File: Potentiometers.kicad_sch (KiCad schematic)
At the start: 14 parts, among them J12 Brake_Sw, J7 Accel_Pot, J9 Brake_Pot

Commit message: Replaced unavailable parts
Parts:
- R14: Mouser Part Number (none) -> 71-CRCW0805100KFKEAC
- R15: Mouser Part Number 71-CRCW080510K0FKEAC -> 71-CRCW08054K99FKEAC
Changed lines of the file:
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@@
 			)
 		)
-		(property "Mouser Part Number" "71-CRCW080510K0FKEAC "
+		(property "Mouser Part Number" "71-CRCW08054K99FKEAC "
 			(at 110.49 80.01 0)
 			(effects
@@
 			)
 		)
-		(property "Mouser Part Number" ""
+		(property "Mouser Part Number" "71-CRCW0805100KFKEAC"
 			(at 93.98 83.82 0)
 			(effects

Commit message: Filled in part numbers, exported BOM and made Excel file for working with it.
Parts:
- C16, C17: P/N (none) -> C0805C104M5R
- D2, D3: P/N (none) -> CDSOT23-T24CAN
- J12: P/N (none) -> 436500215
- J7, J9: P/N (none) -> 436500315
- R14: P/N Inventory -> CRCW0805100KFKEAC
- R15: P/N (none) -> CRCW08054K99FKEAC
- R16, R26, R27: P/N (none) -> CRCW080510K0FKEAC
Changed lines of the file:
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@@
+			)
+		)
+		(property "P/N" "CDSOT23-T24CAN"
+			(at 101.6 83.82 0)
+			(effects
+				(font
+					(size 1.27 1.27)
+				)
+				(hide yes)
 			)
 		)
@@
 			)
 		)
+		(property "P/N" "CDSOT23-T24CAN"
+			(at 101.6 116.84 0)
+			(effects
+				(font
+					(size 1.27 1.27)
+				)
+				(hide yes)
+			)
+		)
 		(pin "2"
 		)
@@
 			)
 		)
+		(property "P/N" "C0805C104M5R"
+			(at 83.82 83.82 0)
+			(effects
+				(font
+					(size 1.27 1.27)
+				)
+				(hide yes)
+			)
+		)
 		(pin "1"
 		)
@@
 			)
 		)
+		(property "P/N" "CRCW080510K0FKEAC "
+			(at 110.49 113.03 0)
+			(effects
+				(font
+					(size 1.27 1.27)
+				)
+				(hide yes)
+			)
+		)
 		(pin "1"
 		)
@@
 			)
 		)
+		(property "P/N" "C0805C104M5R"
+			(at 83.82 116.84 0)
+			(effects
+				(font
+					(size 1.27 1.27)
+				)
+				(hide yes)
+			)
+		)
 		(pin "1"
 		)
@@
 			)
 		)
+		(property "P/N" "CDSOT23-T24CAN"
+			(at 101.6 74.93 0)
+			(effects
+				(font
+					(size 1.27 1.27)
+				)
+				(hide yes)
+			)
+		)
 		(pin "2"
 		)
@@
 			)
 		)
+		(property "P/N" "CDSOT23-T24CAN"
+			(at 101.6 107.95 0)
+			(effects
+				(font
+					(size 1.27 1.27)
+				)
+				(hide yes)
+			)
+		)
 		(pin "2"
 		)
@@
 			)
 		)
+		(property "P/N" "CRCW08054K99FKEAC "
+			(at 110.49 80.01 0)
+			(effects
+				(font
+					(size 1.27 1.27)
+				)
+				(hide yes)
+			)
+		)
 		(pin "1"
 		)
@@
 			)
 		)
-		(property "P/N" "Inventory"
+		(property "P/N" "CRCW0805100KFKEAC"
 			(at 93.98 83.82 0)
 			(effects
@@
 			)
 		)
+		(property "P/N" "CRCW080510K0FKEAC "
+			(at 114.3 147.32 0)
+			(effects
+				(font
+					(size 1.27 1.27)
+				)
+				(hide yes)
+			)
+		)
 		(pin "1"
 		)
@@
 			)
 		)
-		(property "Datasheet" "~"
+		(property "Datasheet" "https://www.molex.com/en-us/products/part-detail/436500215"
 			(at 129.54 138.43 0)
 			(effects
@@
 		)
 		(property "Description" "Generic connector, single row, 01x02, script generated (kicad-library-utils/schlib/autogen/connector/)"
+			(at 129.54 138.43 0)
+			(effects
+				(font
+					(size 1.27 1.27)
+				)
+				(hide yes)
+			)
+		)
+		(property "P/N" "436500215"
 			(at 129.54 138.43 0)
 			(effects
@@
 			)
 		)
-		(property "Datasheet" "~"
+		(property "Datasheet" "https://www.molex.com/molex/search/partSearch?query=436500315&pQuery="
 			(at 144.78 113.03 0)
 			(effects
@@
 		)
 		(property "Vds" ""
+			(at 144.78 113.03 0)
+			(effects
+				(font
+					(size 1.27 1.27)
+				)
+				(hide yes)
+			)
+		)
+		(property "P/N" "436500315"
 			(at 144.78 113.03 0)
 			(effects
@@
 			)
 		)
+		(property "P/N" "CRCW080510K0FKEAC "
+			(at 106.68 140.97 0)
+			(effects
+				(font
+					(size 1.27 1.27)
+				)
+				(hide yes)
+			)
+		)
 		(pin "1"
 		)
@@
 			)
 		)
-		(property "Datasheet" "~"
+		(property "Datasheet" "https://www.molex.com/molex/search/partSearch?query=436500315&pQuery="
 			(at 144.78 80.01 0)
 			(effects
@@
 			(at 144.78 80.01 0)
 			(effects
+				(font
+					(size 1.27 1.27)
+				)
+				(hide yes)
+			)
+		)
+		(property "P/N" "436500315"
+			(at 144.78 80.01 0)
+			(effects

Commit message: Added version update notes.
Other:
- note added: "- Updated accel pot values to increase ADC range - Added brake switch button circuit"
- note removed: "Added brake pot, updated accel pot resistor values"
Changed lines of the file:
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@@
 		)
 	)
-	(text "Added brake pot, updated accel pot resistor values"
+	(text "- Updated accel pot values to increase ADC range\n- Added brake switch button circuit "
 		(exclude_from_sim no)
 		(at 177.8 180.086 0)

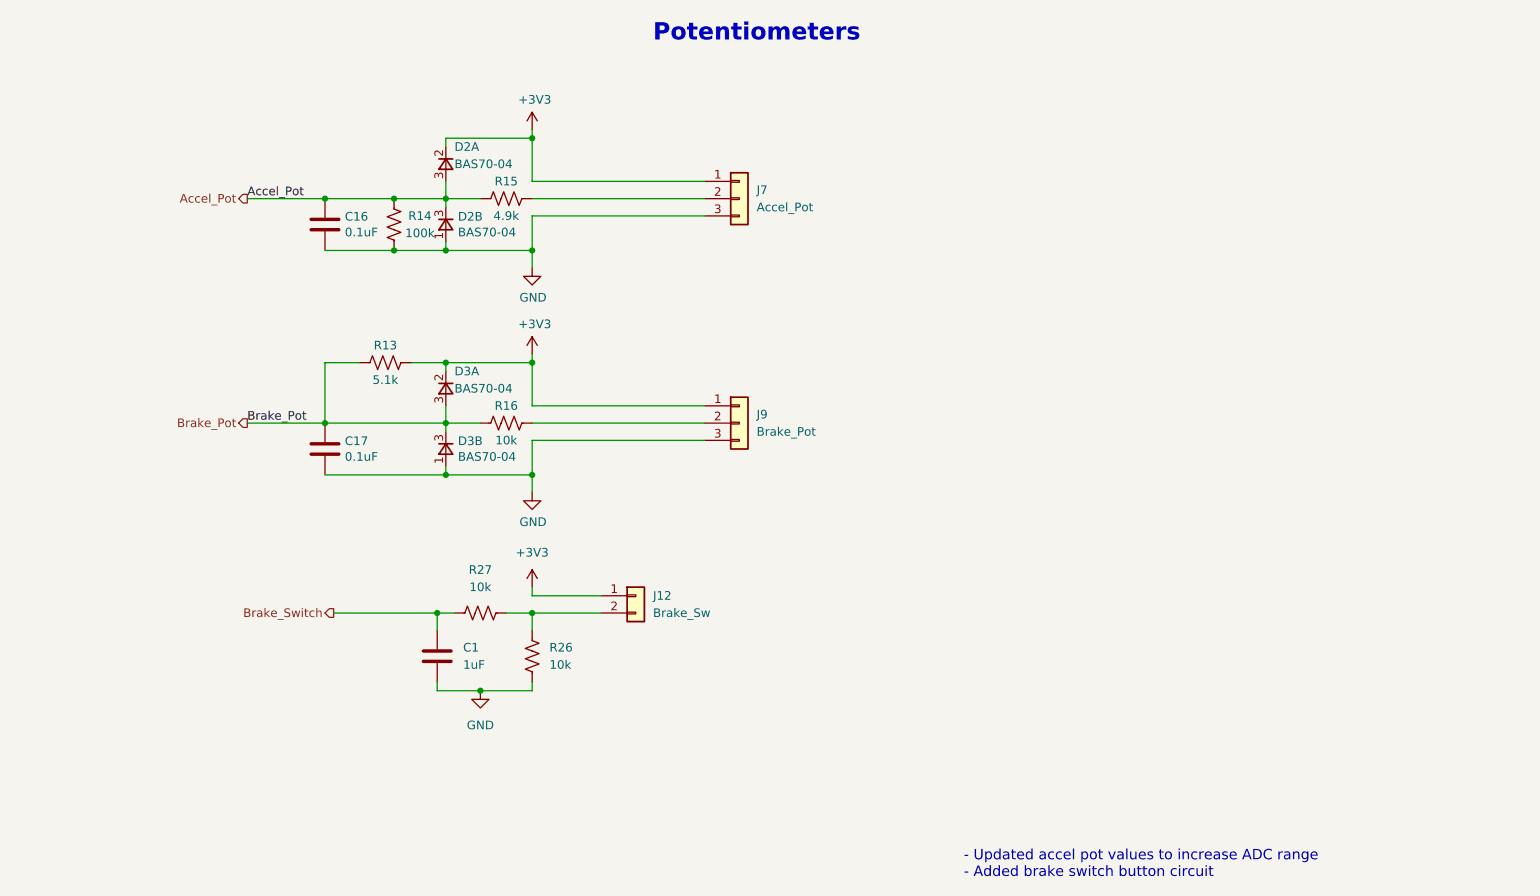
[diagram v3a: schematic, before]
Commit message: Added resistor divider to support 5V potentiometer
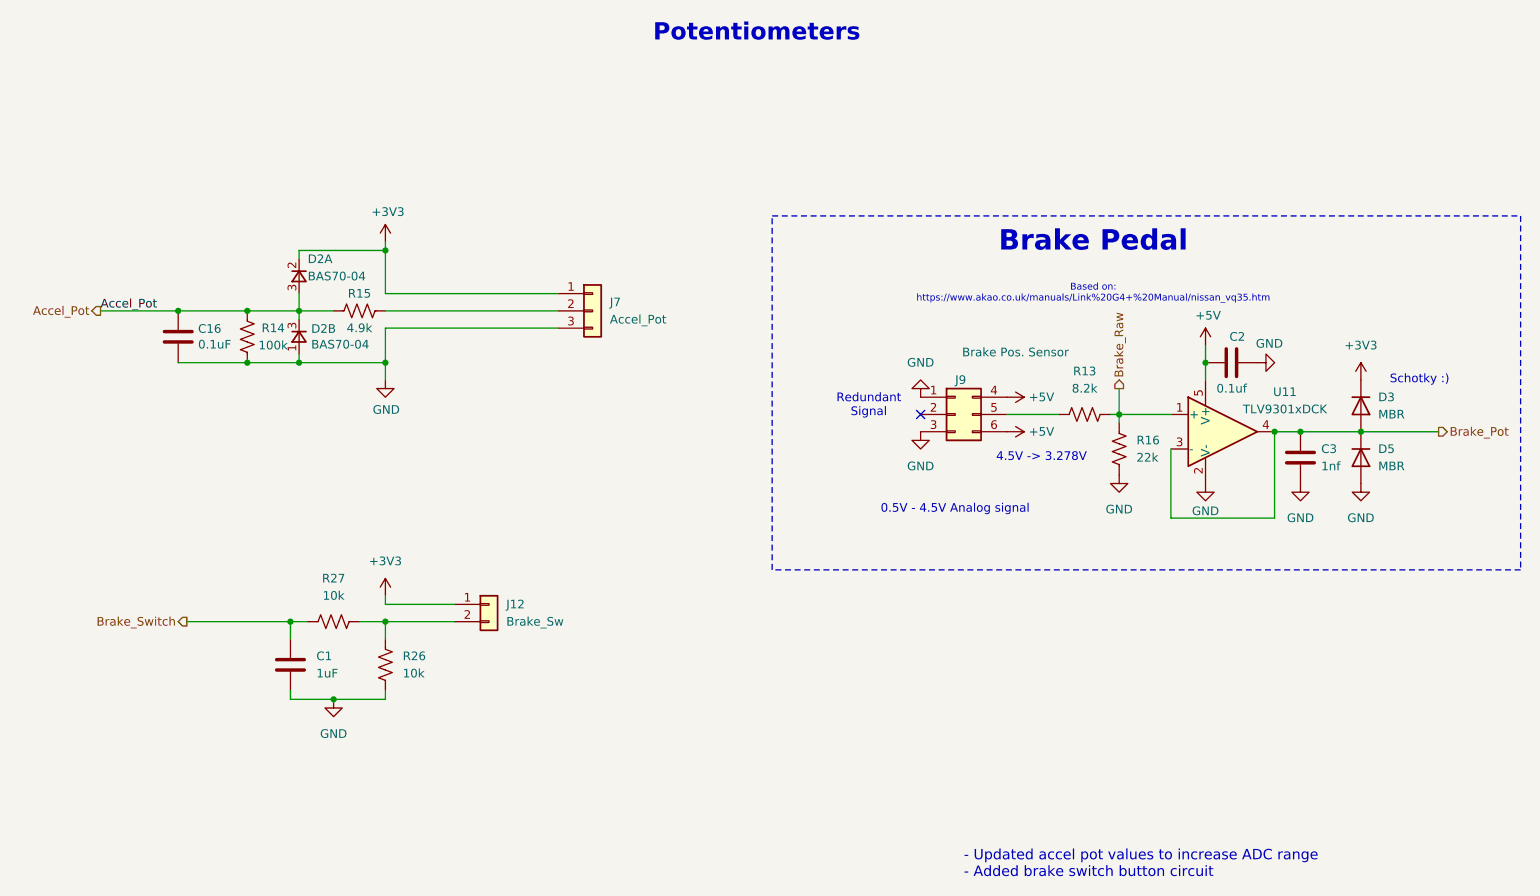
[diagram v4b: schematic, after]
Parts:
- removed C17: 0.1uF, Capacitor_SMD:C_0805_2012Metric, symbol Device:C
- removed D3: BAS70-04, Package_TO_SOT_SMD:SOT-23, symbol utsvt-chips:BAS70-04
- removed J9: Brake_Pot, Connector_Molex:Molex_Micro-Fit_3.0_43650-0315_1x03_P3.00mm_Vertical, symbol Connector_Generic:Conn_01x03
- added C2: 0.1uf, Capacitor_SMD:C_0805_2012Metric, symbol Device:C
- added C3: 1nf, Capacitor_SMD:C_0805_2012Metric, symbol Device:C
- added D3, D5: MBR, Diode_SMD:D_0805_2012Metric, symbol Device:D
- added J9: Brake Pos. Sensor, Connector_Molex:Molex_Micro-Fit_3.0_43045-0612_2x03_P3.00mm_Vertical, symbol Connector_Generic:Conn_02x03_Top_Bottom
- added U11: TLV9301xDCK, Package_TO_SOT_SMD:SOT-353_SC-70-5, symbol Amplifier_Operational:TLV9301xDCK
- R13: value 5.1k -> 8.2k; P/N Inventory -> ERA-3ARB822V
- R16: value 10k -> 22k; Mouser Part Number 71-CRCW080510K0FKEAC -> (none); P/N CRCW080510K0FKEAC -> pickle
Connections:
- net +3V3: now also D3.1 (K); no longer R13.1
- net Brake_Pot: now also C3.2, D3.2 (A), D5.1 (K), U11.3 (-), U11.4; no longer R13.2, R16.2
- net GND: now also R16.2, C2.1, C3.1, D5.2 (A), J9.1 (Pin_1), J9.3 (Pin_3), U11.2 (V-)
- net Brake_Raw: now reaches R16.1
- net Brake_Raw: now also R13.1, U11.1 (+)
- new net: J9.5 (Pin_5), R13.2
- new net +5V: C2.2, J9.4 (Pin_4), J9.6 (Pin_6), U11.5 (V+)
- no-connect marks 0 -> 1
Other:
- note added: "0.5V - 4.5V Analog signal"
- note added: "4.5V -> 3.278V"
- note added: "Based on: https://www.akao.co.uk/manuals/Link%20G4+%20Manual/nissan_vq35.htm"
- note added: "Brake Pedal"
- note added: "Redundant Signal"
- note added: "Schotky :)"
- moved on the sheet: C1, C16, D2A, D2B, J12, J7, R14, R15, R26, R27

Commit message: Removed precharge contactor stuff, made accel 5V instead of 3, removed op amp for brake.
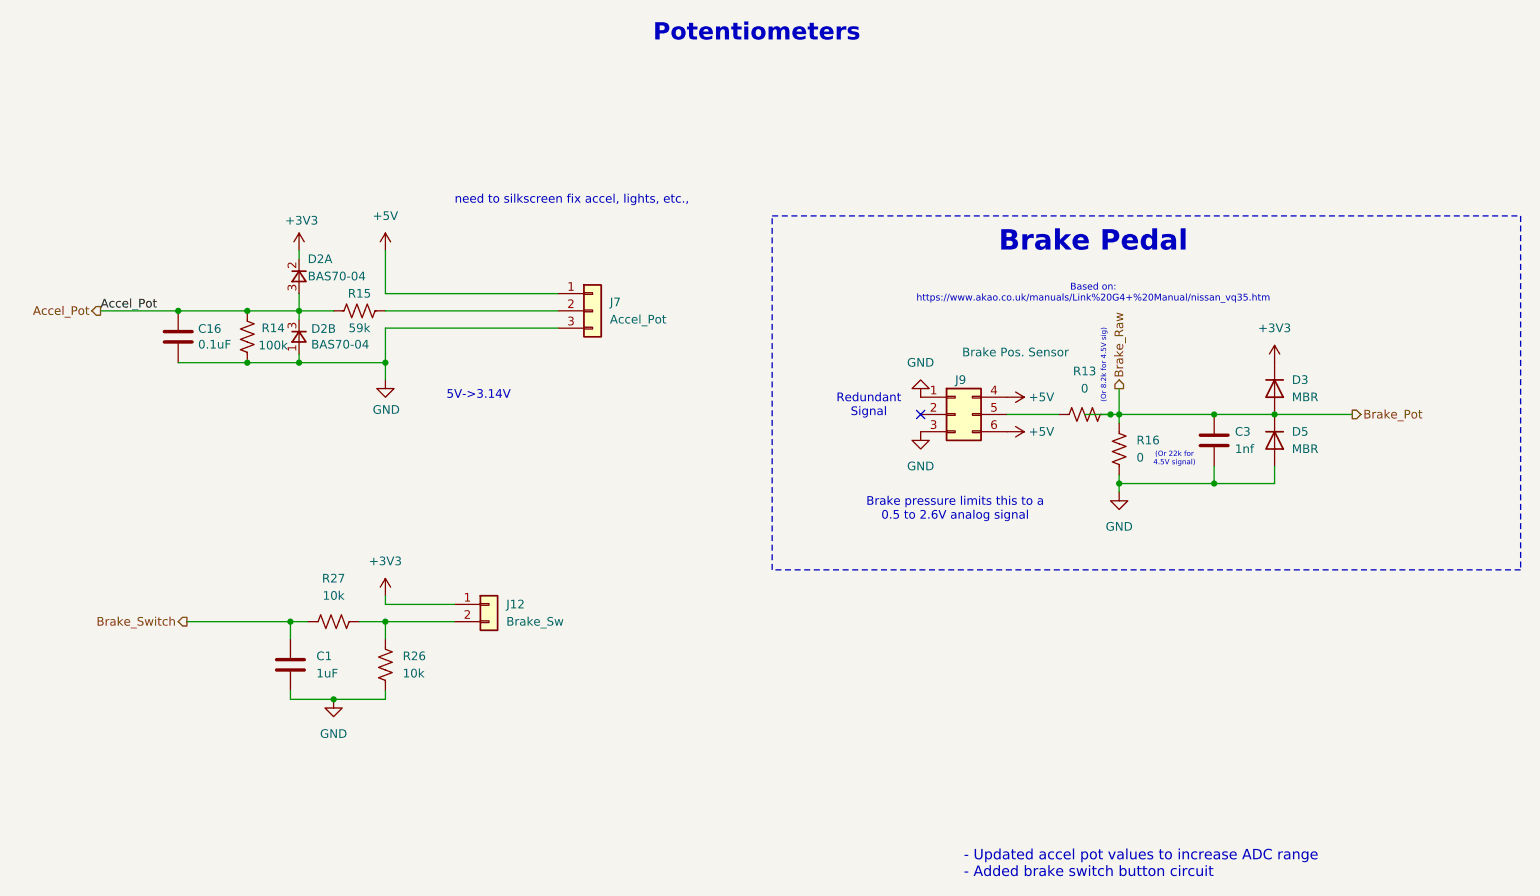
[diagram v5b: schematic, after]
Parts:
- removed C2: 0.1uf, Capacitor_SMD:C_0805_2012Metric, symbol Device:C
- removed U11: TLV9301xDCK, Package_TO_SOT_SMD:SOT-353_SC-70-5, symbol Amplifier_Operational:TLV9301xDCK
- R13: value 8.2k -> 0
- R15: value 4.9k -> 59k
- R16: value 22k -> 0
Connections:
- net Brake_Raw is gone; now on net Brake_Pot: R13.1, R16.1
- net +3V3: no longer J7.1 (Pin_1)
- net +5V: now also J7.1 (Pin_1)
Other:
- note added: "(Or 22k for 4.5V signal)"
- note added: "(Or 8.2k for 4.5V sig)"
- note added: "5V->3.14V"
- note added: "Brake pressure limits this to a 0.5 to 2.6V analog signal"
- note added: "need to silkscreen fix accel, lights, etc.,"
- note removed: "0.5V - 4.5V Analog signal"
- note removed: "4.5V -> 3.278V"
- note removed: "Schotky :)"
- moved on the sheet: C3, D3, D5

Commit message: Layout and routing.
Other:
- moved on the sheet: C3, D3, D5, R16

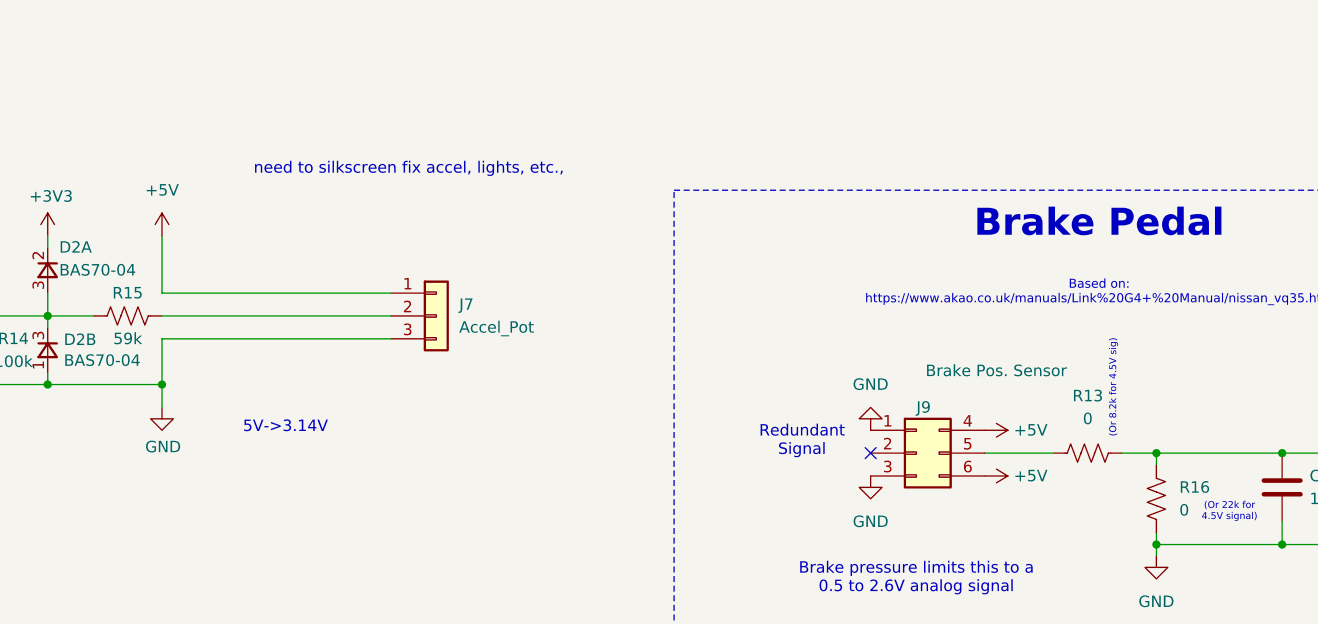
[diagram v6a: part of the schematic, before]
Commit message: More potentiometer TPs.
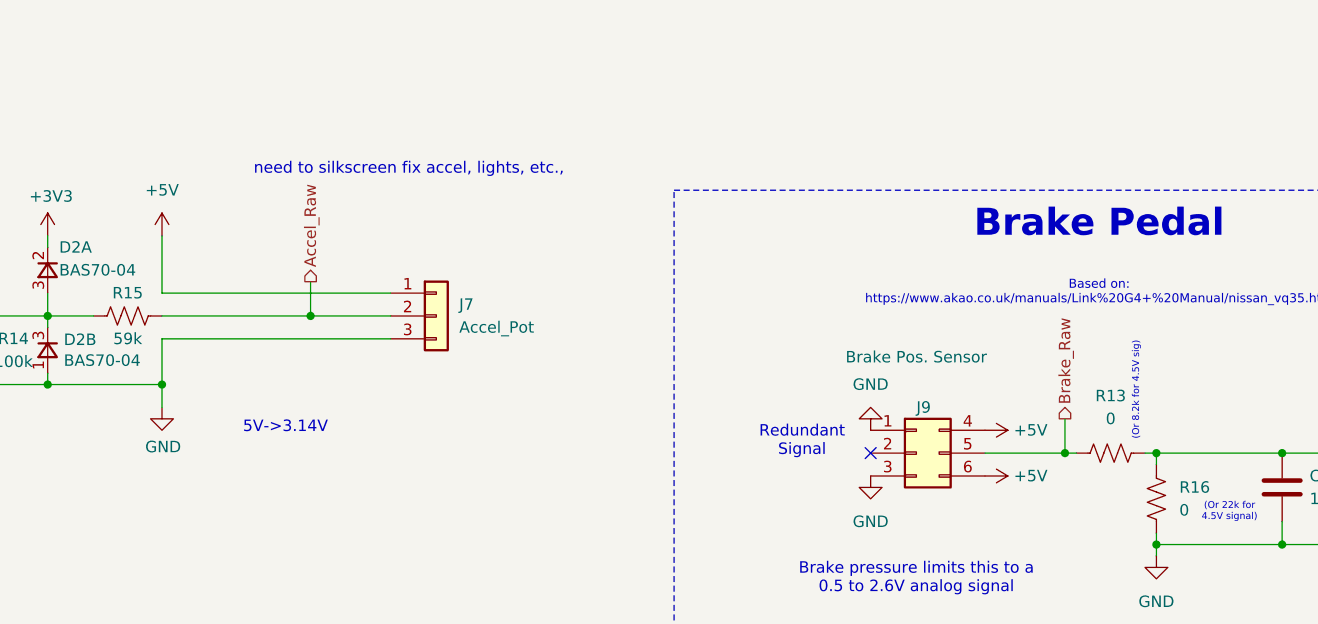
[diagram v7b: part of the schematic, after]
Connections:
- net Accel_Raw: now reaches J7.2 (Pin_2), R15.1
- net Brake_Raw: now reaches J9.5 (Pin_5), R13.2
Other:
- moved on the sheet: R13
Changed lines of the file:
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@@
+	)
+	(junction
+		(at 109.22 96.52)
+		(diameter 0)
+		(color 0 0 0 0)
 	)
 	(junction
@@
 	)
 	(junction
+		(at 193.04 111.76)
+		(diameter 0)
+		(color 0 0 0 0)
+	)
+	(junction
 		(at 80.01 104.14)
 		(diameter 0)
@@
 	(wire
 		(pts
+			(xy 193.04 111.76) (xy 184.15 111.76)
+		)
+		(stroke
+			(width 0)
+			(type default)
+		)
+	)
+	(wire
+		(pts
 			(xy 63.5 142.24) (xy 78.74 142.24)
 		)
@@
 	(wire
 		(pts
+			(xy 109.22 92.71) (xy 109.22 96.52)
+		)
+		(stroke
+			(width 0)
+			(type default)
+		)
+	)
+	(wire
+		(pts
 			(xy 80.01 88.9) (xy 80.01 87.63)
 		)
@@
 	(wire
 		(pts
+			(xy 109.22 96.52) (xy 118.11 96.52)
+		)
+		(stroke
+			(width 0)
+			(type default)
+		)
+	)
+	(wire
+		(pts
 			(xy 81.28 142.24) (xy 78.74 142.24)
 		)
@@
 	(wire
 		(pts
-			(xy 199.39 111.76) (xy 203.2 111.76)
+			(xy 201.93 111.76) (xy 203.2 111.76)
 		)
 		(stroke
@@
 	(wire
 		(pts
-			(xy 191.77 111.76) (xy 184.15 111.76)
+			(xy 194.31 111.76) (xy 193.04 111.76)
 		)
 		(stroke
@@
 	(wire
 		(pts
+			(xy 193.04 107.95) (xy 193.04 111.76)
+		)
+		(stroke
+			(width 0)
+			(type default)
+		)
+	)
+	(wire
+		(pts
 			(xy 92.71 153.67) (xy 92.71 152.4)
 		)
@@
 	(wire
 		(pts
-			(xy 92.71 96.52) (xy 118.11 96.52)
+			(xy 92.71 96.52) (xy 109.22 96.52)
 		)
 		(stroke
@@
 	(text "(Or 8.2k for 4.5V sig)\n"
 		(exclude_from_sim no)
-		(at 198.374 104.648 90)
+		(at 200.914 104.902 90)
 		(effects
 			(font
@@
 		)
 	)
+	(hierarchical_label "Brake_Raw"
+		(shape output)
+		(at 193.04 107.95 90)
+		(fields_autoplaced yes)
+		(effects
+			(font
+				(size 1.27 1.27)
+			)
+			(justify left)
+		)
+	)
+	(hierarchical_label "Accel_Raw"
+		(shape output)
+		(at 109.22 92.71 90)
+		(fields_autoplaced yes)
+		(effects
+			(font
+				(size 1.27 1.27)
+			)
+			(justify left)
+		)
+	)
 	(symbol
 		(lib_id "utsvt-chips:BAS70-04")
@@
 	(symbol
 		(lib_id "Device:R_US")
-		(at 195.58 111.76 270)
+		(at 198.12 111.76 270)
 		(unit 1)
 		(exclude_from_sim no)
@@
 		(fields_autoplaced yes)
 		(property "Reference" "R13"
-			(at 195.58 105.41 90)
+			(at 198.12 105.41 90)
 			(effects
 				(font
@@
 		)
 		(property "Value" "0"
-			(at 195.58 107.95 90)
+			(at 198.12 107.95 90)
 			(effects
 				(font
@@
 		)
 		(property "Footprint" "Resistor_SMD:R_0805_2012Metric"
-			(at 195.326 112.776 90)
+			(at 197.866 112.776 90)
 			(effects
 				(font
@@
 		)
 		(property "Datasheet" "~"
-			(at 195.58 111.76 0)
+			(at 198.12 111.76 0)
 			(effects
 				(font
@@
 		)
 		(property "Description" "Resistor, US symbol"
-			(at 195.58 111.76 0)
+			(at 198.12 111.76 0)
 			(effects
 				(font
@@
 		)
 		(property "P/N" "ERA-3ARB822V"
-			(at 195.58 111.76 0)
+			(at 198.12 111.76 0)
 			(effects
 				(font
@@
 		)
 		(property "Value" "Brake Pos. Sensor"
-			(at 177.546 102.616 0)
-			(effects
-				(font
+			(at 168.656 101.092 0)
+			(effects
+				(font
